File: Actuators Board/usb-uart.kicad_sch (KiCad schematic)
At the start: 20 parts, among them J3 USB_C_Receptacle_USB2.0, U3 INTERFACE-CP2102-GMR(QFN28), U6 AZ1084-3.3

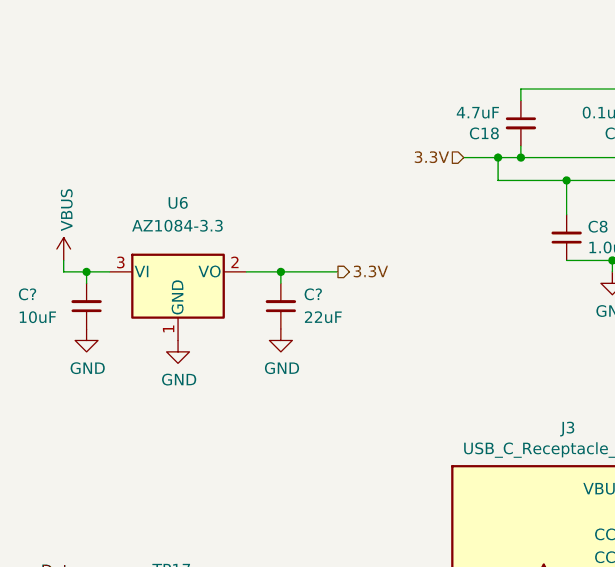
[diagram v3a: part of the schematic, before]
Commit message: Footprint assignments for capacitors+changed resistors on solenoid FET
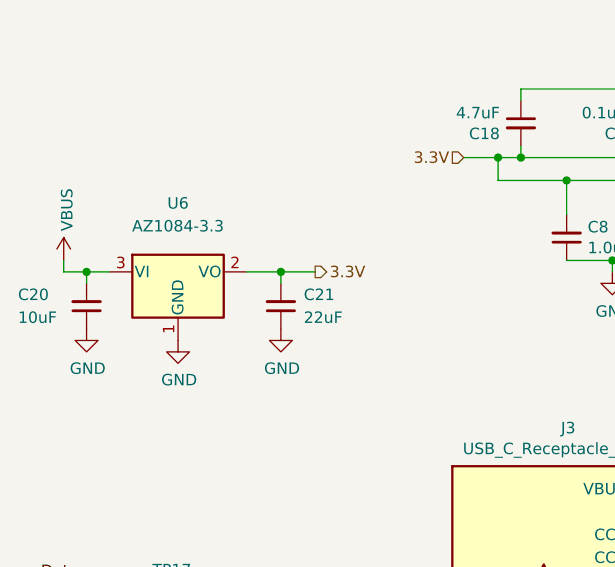
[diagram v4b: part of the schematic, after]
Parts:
- C20, C21: renamed from C?; footprint (none) -> Capacitor_SMD:C_0603_1608Metric
- R3: footprint (none) -> Resistor_SMD:R_0603_1608Metric
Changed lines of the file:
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@@
     (stroke (width 0) (type default) (color 0 0 0 0))
   )
-  (wire (pts (xy 71.12 64.77) (xy 77.47 64.77))
+  (wire (pts (xy 71.12 64.77) (xy 74.93 64.77))
     (stroke (width 0) (type default) (color 0 0 0 0))
   )
@@
     (effects (font (size 1.27 1.27)) (justify left))
   )
-  (hierarchical_label "3.3V" (shape output) (at 77.47 64.77 0)
+  (hierarchical_label "3.3V" (shape output) (at 74.93 64.77 0)
     (effects (font (size 1.27 1.27)) (justify left))
   )
@@
       (effects (font (size 1.27 1.27)) (justify left))
     )
-    (property "Footprint" "" (id 2) (at 128.27 69.85 0)
+    (property "Footprint" "Resistor_SMD:R_0603_1608Metric" (id 2) (at 128.27 69.85 0)
       (effects (font (size 1.27 1.27)) hide)
     )
@@
   (symbol (lib_id "power:GND") (at 71.12 71.12 0) (unit 1)
     (in_bom yes) (on_board yes)
-    (property "Reference" "#PWR?" (id 0) (at 71.12 77.47 0)
+    (property "Reference" "#PWR0146" (id 0) (at 71.12 77.47 0)
       (effects (font (size 1.27 1.27)) hide)
     )
@@
   (symbol (lib_id "Device:C_Small") (at 49.53 68.58 180) (unit 1)
     (in_bom yes) (on_board yes)
-    (property "Reference" "C?" (id 0) (at 41.91 67.31 0)
+    (property "Reference" "C20" (id 0) (at 41.91 67.31 0)
       (effects (font (size 1.27 1.27)) (justify right))
     )
@@
       (effects (font (size 1.27 1.27)) (justify right))
     )
-    (property "Footprint" "" (id 2) (at 49.53 68.58 0)
+    (property "Footprint" "Capacitor_SMD:C_0603_1608Metric" (id 2) (at 49.53 68.58 0)
       (effects (font (size 1.27 1.27)) hide)
     )
@@
   (symbol (lib_id "Device:C_Small") (at 71.12 68.58 180) (unit 1)
     (in_bom yes) (on_board yes)
-    (property "Reference" "C?" (id 0) (at 73.66 67.31 0)
+    (property "Reference" "C21" (id 0) (at 73.66 67.31 0)
       (effects (font (size 1.27 1.27)) (justify right))
     )
@@
       (effects (font (size 1.27 1.27)) (justify right))
     )
-    (property "Footprint" "" (id 2) (at 71.12 68.58 0)
+    (property "Footprint" "Capacitor_SMD:C_0603_1608Metric" (id 2) (at 71.12 68.58 0)
       (effects (font (size 1.27 1.27)) hide)
     )
@@
   (symbol (lib_id "power:GND") (at 49.53 71.12 0) (unit 1)
     (in_bom yes) (on_board yes)
-    (property "Reference" "#PWR?" (id 0) (at 49.53 77.47 0)
-      (effects (font (size 1.27 1.27)) hide)
-    )
+    (property "Reference" "#PWR0145" (id 0) (at 49.53 77.47 0)
+      (effects (font (size 1.27 1.27)) hide)
+    )

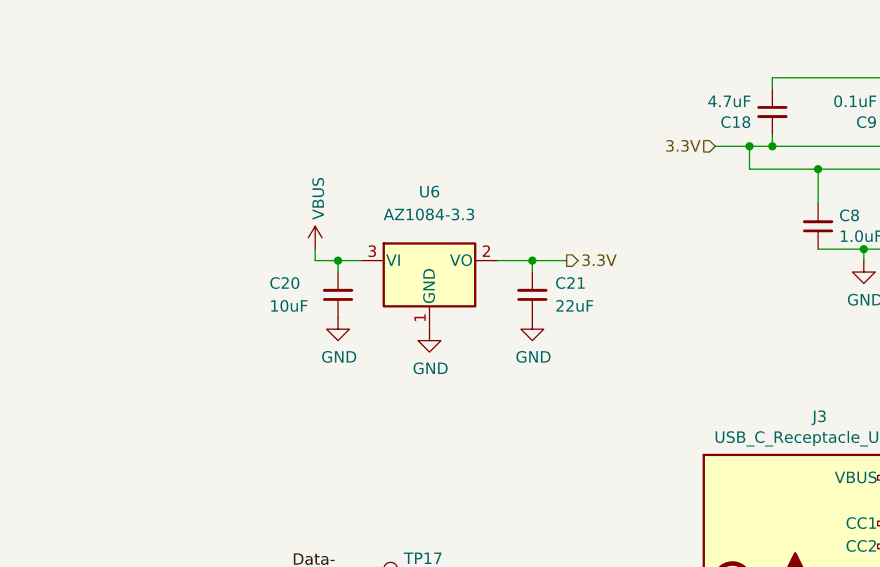
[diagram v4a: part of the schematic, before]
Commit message: ideal diode added
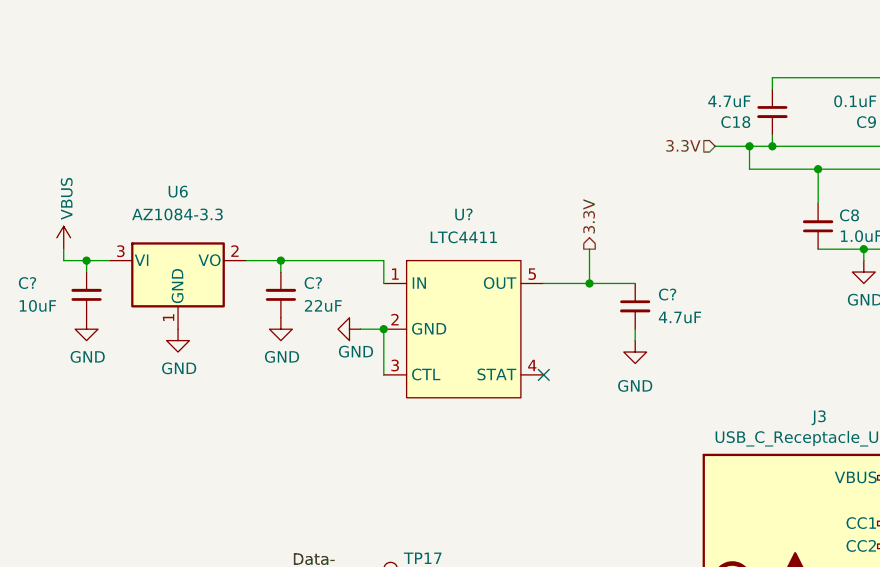
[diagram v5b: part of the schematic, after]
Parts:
- added C?: 4.7uF, symbol Device:C_Small
- added U?: LTC4411, symbol iclr:LTC4411
- C?: renamed from C20; footprint Capacitor_SMD:C_0603_1608Metric -> (none)
- C?: renamed from C21; footprint Capacitor_SMD:C_0603_1608Metric -> (none)
- R3: footprint Resistor_SMD:R_0603_1608Metric -> (none)
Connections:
- net 3.3V: now also C?.1, U?.5 (OUT); no longer C?.2, U6.2 (VO)
- net GND: now also C?.2, U?.2 (GND), U?.3 (CTL)
- new net: C?.2, U6.2 (VO), U?.1 (IN)
- no-connect marks 20 -> 21
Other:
- moved on the sheet: C?, U6

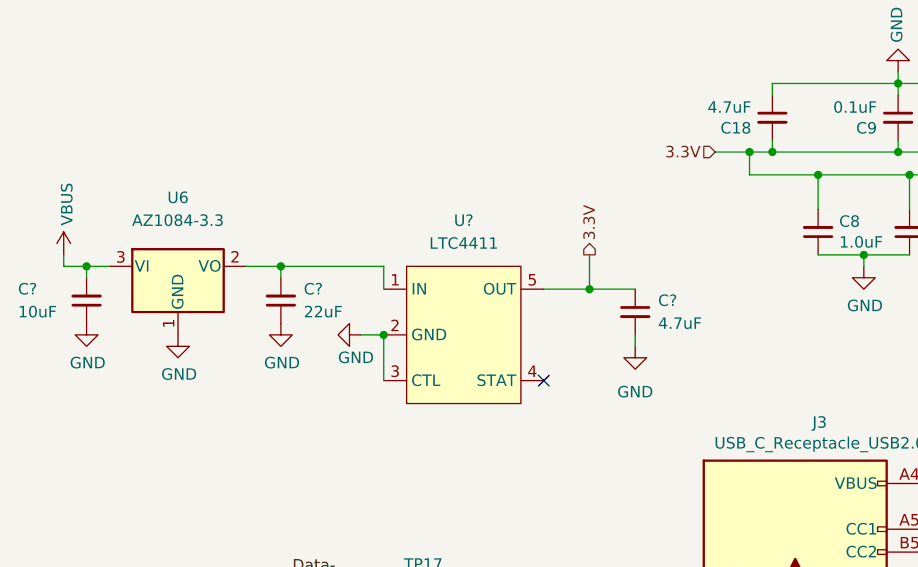
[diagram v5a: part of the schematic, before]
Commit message: Manual merge of ideal diodes and footprint changes
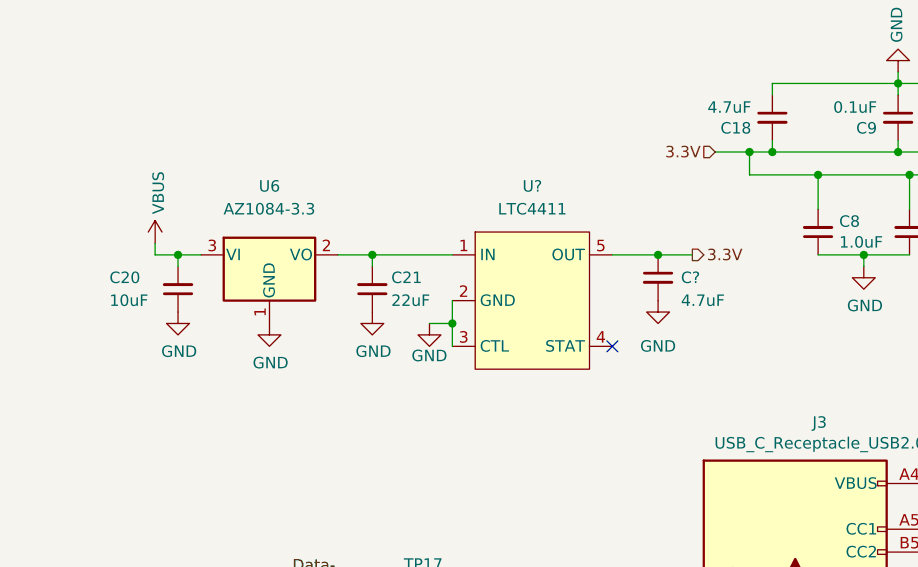
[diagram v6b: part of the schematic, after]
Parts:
- removed C?: 4.7uF, symbol Device:C_Small
- removed U?: LTC4411, symbol iclr:LTC4411
- added C?: 4.7uF, symbol Device:C_Small
- added U?: LTC4411, symbol iclr:LTC4411
- C20, C21: renamed from C?; footprint (none) -> Capacitor_SMD:C_0603_1608Metric
- R3: footprint (none) -> Resistor_SMD:R_0603_1608Metric
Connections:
- net 3.3V: now also C?.1, U?.5 (OUT)
- net GND: now also C?.2, U?.2 (GND), U?.3 (CTL)
- net at C21.2, U6.2 (VO): now also U?.1 (IN)
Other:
- moved on the sheet: C20, C21, U6

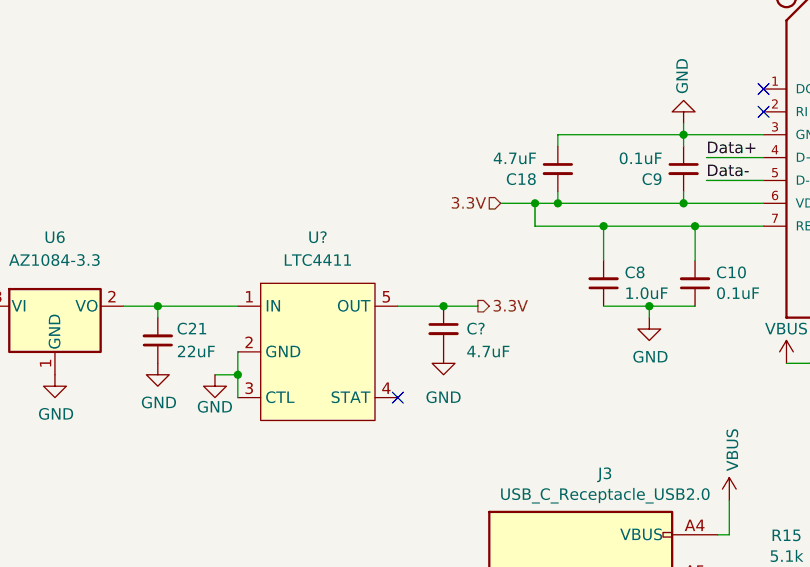
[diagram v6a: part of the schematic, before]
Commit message: Annotated schematic and imported changes into PCB
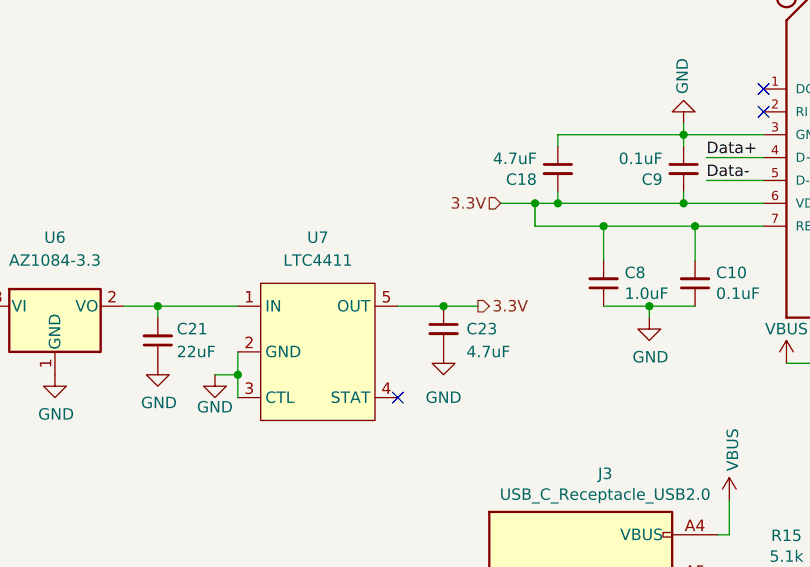
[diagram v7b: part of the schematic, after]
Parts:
- C23: renamed from C?; footprint (none) -> Capacitor_SMD:C_0603_1608Metric
- U7: renamed from U?; footprint (none) -> Package_TO_SOT_SMD:SOT-23-5
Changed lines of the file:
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@@
   (symbol (lib_id "iclr:LTC4411") (at 71.12 58.42 0) (unit 1)
     (in_bom yes) (on_board yes) (fields_autoplaced)
-    (property "Reference" "U?" (id 0) (at 71.12 55.88 0))
+    (property "Reference" "U7" (id 0) (at 71.12 55.88 0))
     (property "Value" "LTC4411" (id 1) (at 71.12 58.42 0))
-    (property "Footprint" "" (id 2) (at 71.12 58.42 0)
+    (property "Footprint" "Package_TO_SOT_SMD:SOT-23-5" (id 2) (at 71.12 58.42 0)
       (effects (font (size 1.27 1.27)) hide)
     )
@@
   (symbol (lib_id "power:GND") (at 59.69 71.12 0) (unit 1)
     (in_bom yes) (on_board yes)
-    (property "Reference" "#PWR?" (id 0) (at 59.69 77.47 0)
+    (property "Reference" "#PWR0150" (id 0) (at 59.69 77.47 0)
       (effects (font (size 1.27 1.27)) hide)
     )
@@
   (symbol (lib_id "power:GND") (at 85.09 68.58 0) (unit 1)
     (in_bom yes) (on_board yes) (fields_autoplaced)
-    (property "Reference" "#PWR?" (id 0) (at 85.09 74.93 0)
+    (property "Reference" "#PWR0149" (id 0) (at 85.09 74.93 0)
       (effects (font (size 1.27 1.27)) hide)
     )
@@
   (symbol (lib_id "Device:C_Small") (at 85.09 66.04 0) (unit 1)
     (in_bom yes) (on_board yes)
-    (property "Reference" "C?" (id 0) (at 87.63 66.04 0)
+    (property "Reference" "C23" (id 0) (at 87.63 66.04 0)
       (effects (font (size 1.27 1.27)) (justify left))
     )
@@
       (effects (font (size 1.27 1.27)) (justify left))
     )
-    (property "Footprint" "" (id 2) (at 85.09 66.04 0)
+    (property "Footprint" "Capacitor_SMD:C_0603_1608Metric" (id 2) (at 85.09 66.04 0)
       (effects (font (size 1.27 1.27)) hide)
     )

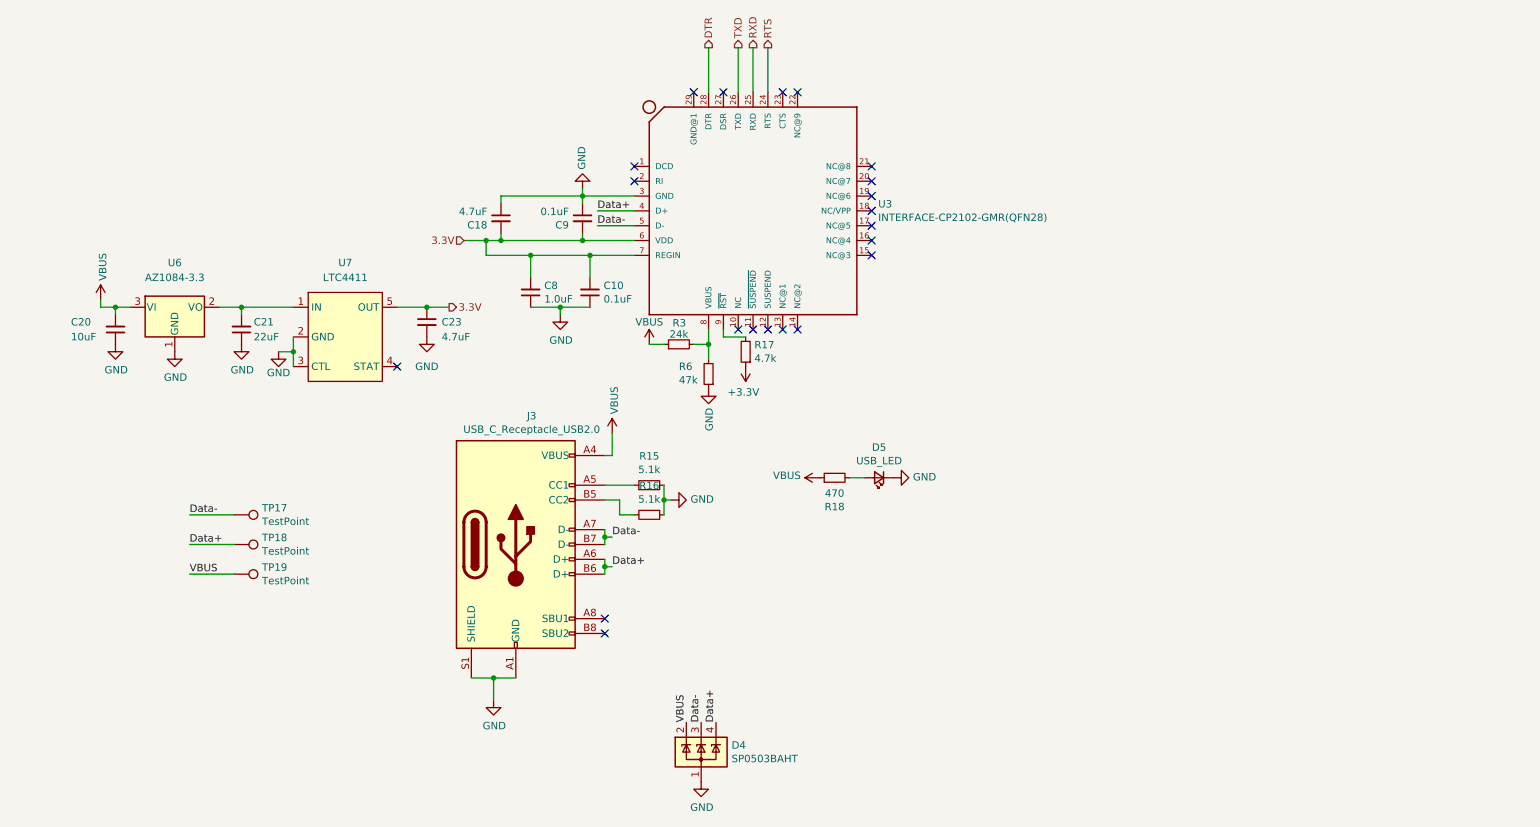
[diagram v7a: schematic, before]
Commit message: Swapped LDO to RT9025-25GSP & moved components closer together
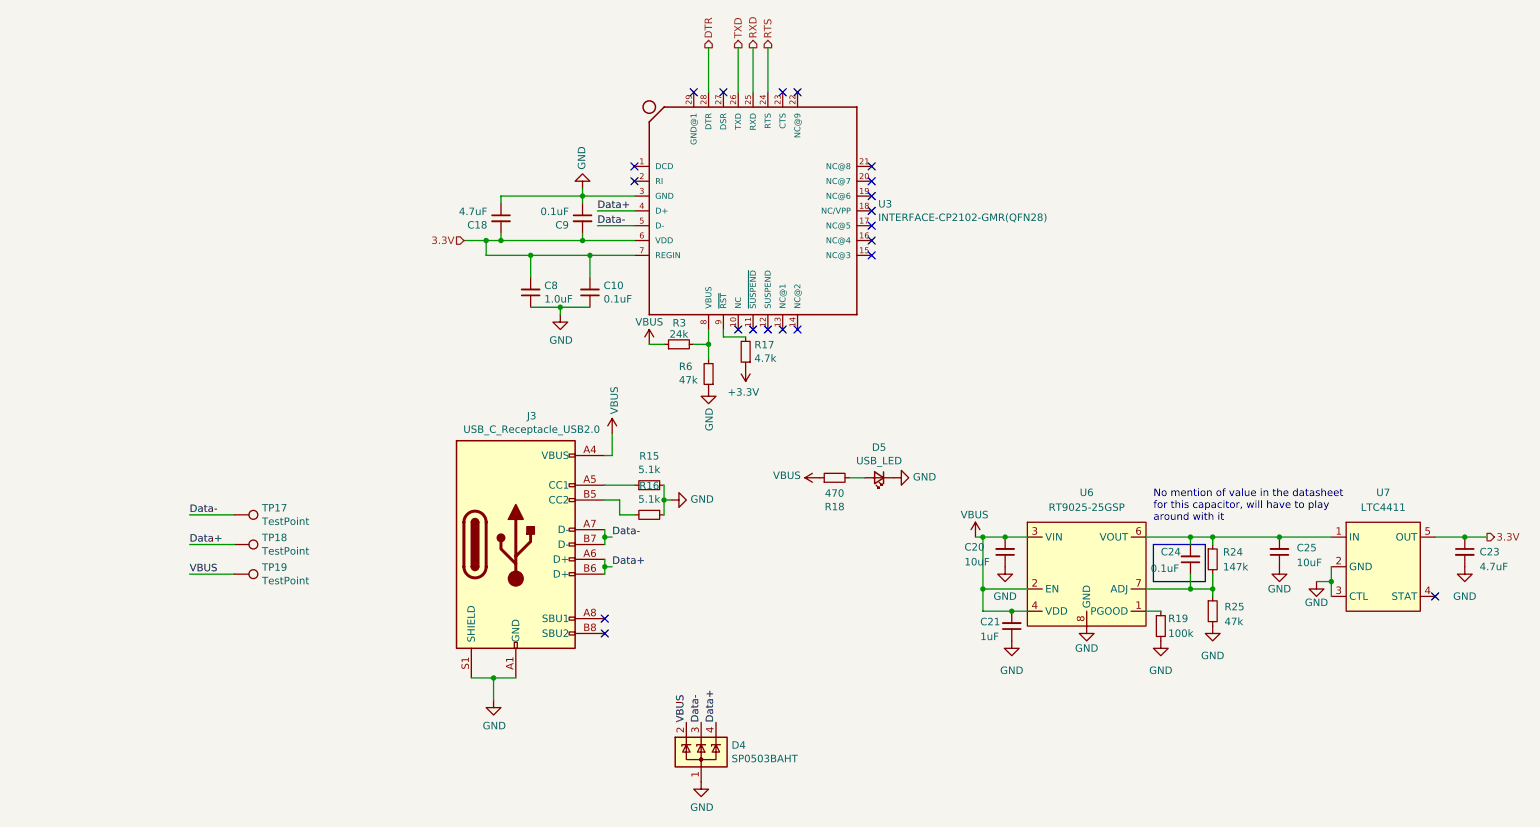
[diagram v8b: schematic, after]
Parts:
- removed U6: AZ1084-3.3, Package_TO_SOT_SMD:TO-252-3_TabPin2, symbol Regulator_Linear:AZ1084-3.3
- added C24: 0.1uF, Capacitor_SMD:C_0603_1608Metric, symbol Device:C_Small
- added C25: 10uF, Capacitor_SMD:C_0603_1608Metric, symbol Device:C_Small
- added R19: 100k, Resistor_SMD:R_0603_1608Metric, symbol Device:R_Small
- added R24: 147k, Resistor_SMD:R_0603_1608Metric, symbol Device:R_Small
- added R25: 47k, Resistor_SMD:R_0603_1608Metric, symbol Device:R_Small
- added U6: RT9025-25GSP, Package_SO:SOP-8_3.9x4.9mm_P1.27mm, symbol iclr:RT9025-25GSP
- C21: value 22uF -> 1uF
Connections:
- net GND: now also C25.1, R19.2, R25.2, U6.8 (GND)
- net VBUS: now also C21.2, U6.2 (EN), U6.3 (VIN), U6.4 (VDD)
- net at U7.1 (IN): now also C24.2, C25.2, R24.1, U6.6 (VOUT); no longer C21.2
- new net: R19.1, U6.1 (PGOOD)
- new net: C24.1, R24.2, R25.1, U6.7 (ADJ)
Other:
- note added: "No mention of value in the datasheet for this capacitor, will have to play around with it"
- moved on the sheet: C23, U7
